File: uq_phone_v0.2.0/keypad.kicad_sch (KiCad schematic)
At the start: 71 parts, among them SW1 SKTAAAE010, SW10 SKTAAAE010, SW11 SKTAAAE010, SW12 SKTAAAE010, SW13 SKTAAAE010, SW14 SKTAAAE010, SW15 SKTAAAE010, SW16 SKSCLCE010, SW17 SKTAAAE010, SW18 SKTAAAE010, SW19 SKTAAAE010, SW2 SKTAAAE010, SW20 SKTAAAE010, SW21 SKTAAAE010, SW22 SKSCLCE010, SW23 SKTAAAE010, SW24 SKTAAAE010, SW25 SKTAAAE010, SW26 SKTAAAE010, SW27 SKTAAAE010, SW28 SKTAAAE010, SW29 SKTAAAE010, SW3 SKTAAAE010, SW30 SKTAAAE010, SW31 SKTAAAE010, SW32 SKTAAAE010, SW33 SKTAAAE010, SW34 SKTAAAE010, SW35 SKTAAAE010, SW36 SKTAAAE010, SW37 SKTAAAE010, SW38 SKTAAAE010, SW39 SKTAAAE010, SW4 SKTAAAE010, SW40 SKTAAAE010, SW41 SKTAAAE010, SW5 SKTAAAE010, SW6 SKSCLCE010, SW7 SKTAAAE010, SW8 SKTAAAE010, SW9 SKTAAAE010

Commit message: More routing and moving cellular to new project
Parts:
- LED18, LED19, LED20, LED21, LED22, LED23, LED24, LED25, LED26, LED27, LED28, LED31: now fitted
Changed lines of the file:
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@@
 		(in_bom yes)
 		(on_board yes)
-		(dnp yes)
+		(dnp no)
 		(property "Reference" "LED27"
 			(at 300.482 133.096 0)
@@
 		(in_bom yes)
 		(on_board yes)
-		(dnp yes)
+		(dnp no)
 		(fields_autoplaced yes)
 		(property "Reference" "#PWR0199"
@@
 		(in_bom yes)
 		(on_board yes)
-		(dnp yes)
+		(dnp no)
 		(property "Reference" "#PWR0212"
 			(at 313.69 129.54 0)
@@
 		(in_bom yes)
 		(on_board yes)
-		(dnp yes)
+		(dnp no)
 		(fields_autoplaced yes)
 		(property "Reference" "#PWR0201"
@@
 		(in_bom yes)
 		(on_board yes)
-		(dnp yes)
+		(dnp no)
 		(property "Reference" "#PWR0197"
 			(at 292.1 105.41 0)
@@
 		(in_bom yes)
 		(on_board yes)
-		(dnp yes)
+		(dnp no)
 		(fields_autoplaced yes)
 		(property "Reference" "#PWR0193"
@@
 		(in_bom yes)
 		(on_board yes)
-		(dnp yes)
+		(dnp no)
 		(property "Reference" "#PWR0218"
 			(at 313.69 153.67 0)
@@
 		(in_bom yes)
 		(on_board yes)
-		(dnp yes)
+		(dnp no)
 		(property "Reference" "#PWR0191"
 			(at 270.51 81.28 0)
@@
 		(in_bom yes)
 		(on_board yes)
-		(dnp yes)
+		(dnp no)
 		(property "Reference" "#PWR0208"
 			(at 292.1 129.54 0)
@@
 		(in_bom yes)
 		(on_board yes)
-		(dnp yes)
+		(dnp no)
 		(property "Reference" "LED25"
 			(at 322.072 108.966 0)
@@
 		(in_bom yes)
 		(on_board yes)
-		(dnp yes)
+		(dnp no)
 		(fields_autoplaced yes)
 		(property "Reference" "#PWR0200"
@@
 		(in_bom yes)
 		(on_board yes)
-		(dnp yes)
+		(dnp no)
 		(property "Reference" "#PWR0216"
 			(at 270.51 153.67 0)
@@
 		(in_bom yes)
 		(on_board yes)
-		(dnp yes)
+		(dnp no)
 		(property "Reference" "#PWR0217"
 			(at 292.1 153.67 0)
@@
 		(in_bom yes)
 		(on_board yes)
-		(dnp yes)
+		(dnp no)
 		(property "Reference" "LED23"
 			(at 278.892 108.966 0)
@@
 		(in_bom yes)
 		(on_board yes)
-		(dnp yes)
+		(dnp no)
 		(fields_autoplaced yes)
 		(property "Reference" "#PWR077"
@@
 		(in_bom yes)
 		(on_board yes)
-		(dnp yes)
+		(dnp no)
 		(property "Reference" "LED19"
 			(at 300.482 60.706 0)
@@
 		(in_bom yes)
 		(on_board yes)
-		(dnp yes)
+		(dnp no)
 		(property "Reference" "LED18"
 			(at 278.892 60.706 0)
@@
 		(in_bom yes)
 		(on_board yes)
-		(dnp yes)
+		(dnp no)
 		(fields_autoplaced yes)
 		(property "Reference" "#PWR0215"
@@
 		(in_bom yes)
 		(on_board yes)
-		(dnp yes)
+		(dnp no)
 		(property "Reference" "#PWR0198"
 			(at 313.69 105.41 0)
@@
 		(in_bom yes)
 		(on_board yes)
-		(dnp yes)
+		(dnp no)
 		(property "Reference" "LED24"
 			(at 300.482 108.966 0)
@@
 		(in_bom yes)
 		(on_board yes)
-		(dnp yes)
+		(dnp no)
 		(property "Reference" "LED26"
 			(at 278.892 133.096 0)
@@
 		(in_bom yes)
 		(on_board yes)
-		(dnp yes)
+		(dnp no)
 		(property "Reference" "#PWR0224"
 			(at 313.69 177.8 0)
@@
 		(in_bom yes)
 		(on_board yes)
-		(dnp yes)
+		(dnp no)
 		(fields_autoplaced yes)
 		(property "Reference" "#PWR0213"
@@
 		(in_bom yes)
 		(on_board yes)
-		(dnp yes)
+		(dnp no)
 		(property "Reference" "LED22"
 			(at 322.072 84.836 0)
@@
 		(in_bom yes)
 		(on_board yes)
-		(dnp yes)
+		(dnp no)
 		(fields_autoplaced yes)
 		(property "Reference" "#PWR0214"
@@
 		(in_bom yes)
 		(on_board yes)
-		(dnp yes)
+		(dnp no)
 		(property "Reference" "#PWR0202"
 			(at 270.51 129.54 0)
@@
 		(in_bom yes)
 		(on_board yes)
-		(dnp yes)
+		(dnp no)
 		(property "Reference" "LED28"
 			(at 322.072 133.096 0)
@@
 		(in_bom yes)
 		(on_board yes)
-		(dnp yes)
+		(dnp no)
 		(fields_autoplaced yes)
 		(property "Reference" "#PWR0192"
@@
 		(in_bom yes)
 		(on_board yes)
-		(dnp yes)
+		(dnp no)
 		(fields_autoplaced yes)
 		(property "Reference" "#PWR0221"
@@
 		(in_bom yes)
 		(on_board yes)
-		(dnp yes)
+		(dnp no)
 		(fields_autoplaced yes)
 		(property "Reference" "#PWR0194"
@@
 		(in_bom yes)
 		(on_board yes)
-		(dnp yes)
+		(dnp no)
 		(property "Reference" "LED31"
 			(at 322.072 157.226 0)
@@
 		(in_bom yes)
 		(on_board yes)
-		(dnp yes)
+		(dnp no)
 		(property "Reference" "#PWR0182"
 			(at 292.1 81.28 0)
@@
 		(in_bom yes)
 		(on_board yes)
-		(dnp yes)
+		(dnp no)
 		(property "Reference" "LED20"
 			(at 278.892 84.836 0)
@@
 		(in_bom yes)
 		(on_board yes)
-		(dnp yes)
+		(dnp no)
 		(property "Reference" "LED21"
 			(at 300.482 84.836 0)
@@
 		(in_bom yes)
 		(on_board yes)
-		(dnp yes)
+		(dnp no)
 		(fields_autoplaced yes)
 		(property "Reference" "#PWR0195"
@@
 		(in_bom yes)
 		(on_board yes)
-		(dnp yes)
+		(dnp no)
 		(property "Reference" "#PWR0196"
 			(at 270.51 105.41 0)

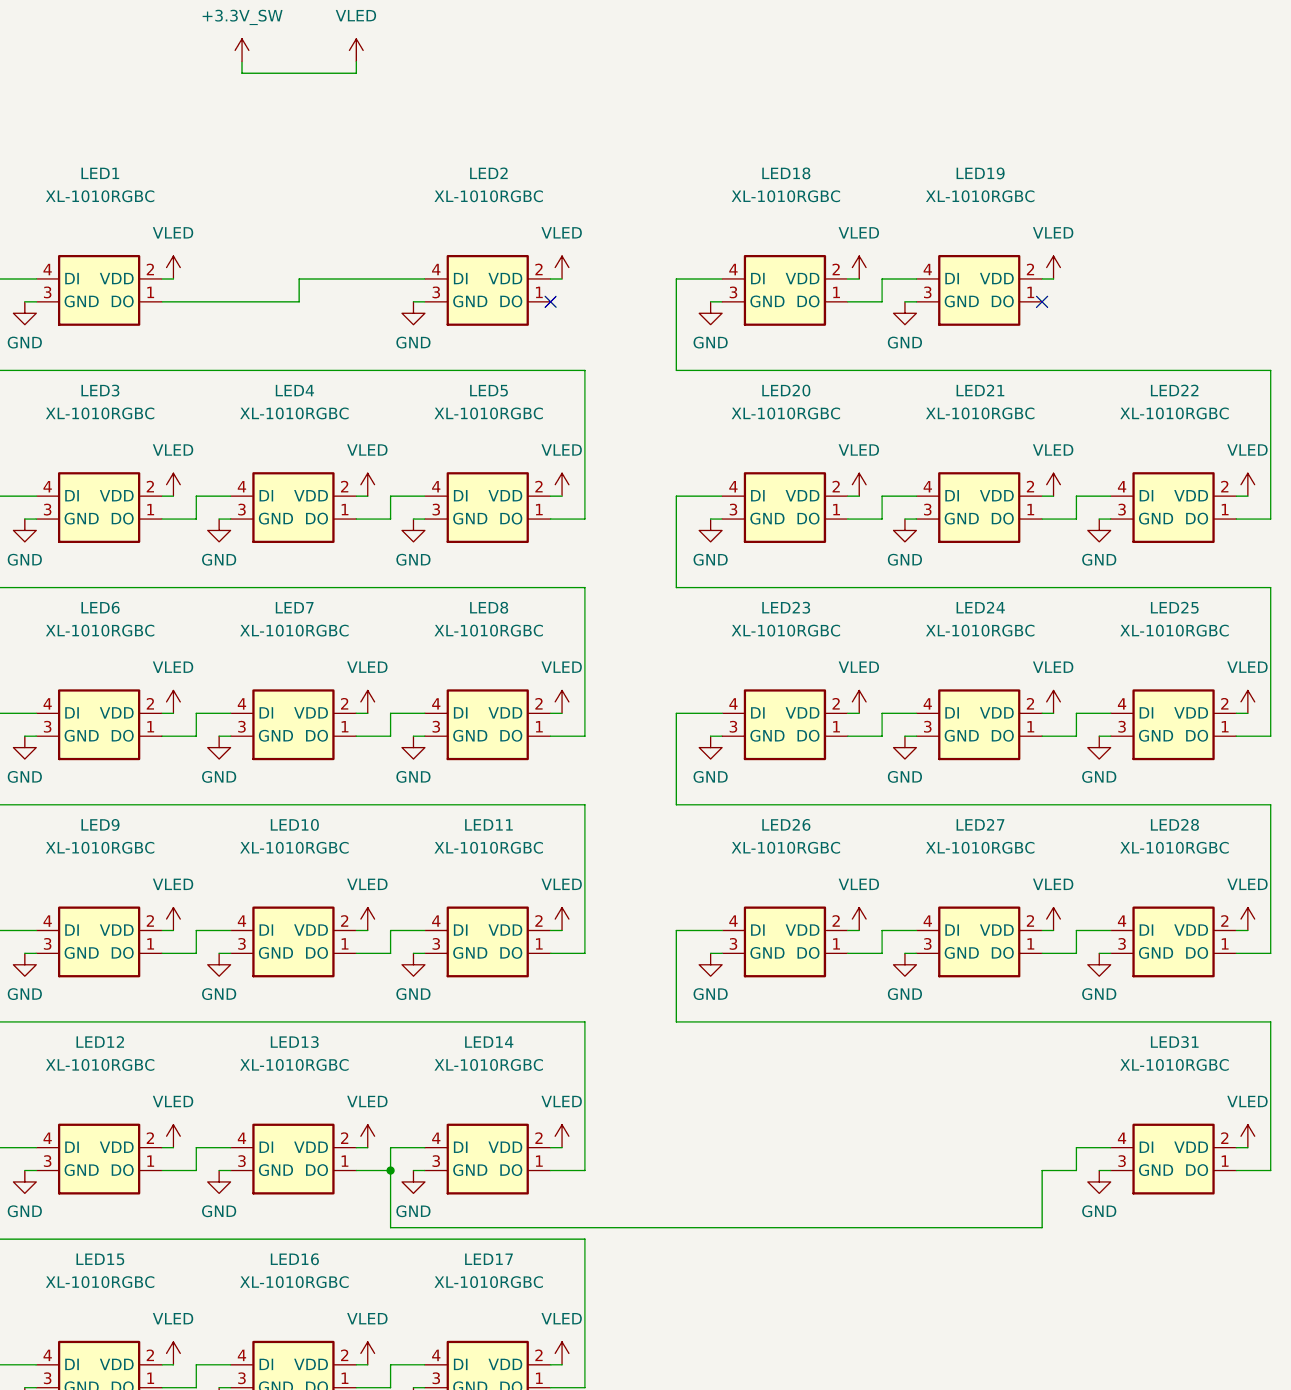
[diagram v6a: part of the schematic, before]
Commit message: New HP jack and circuit
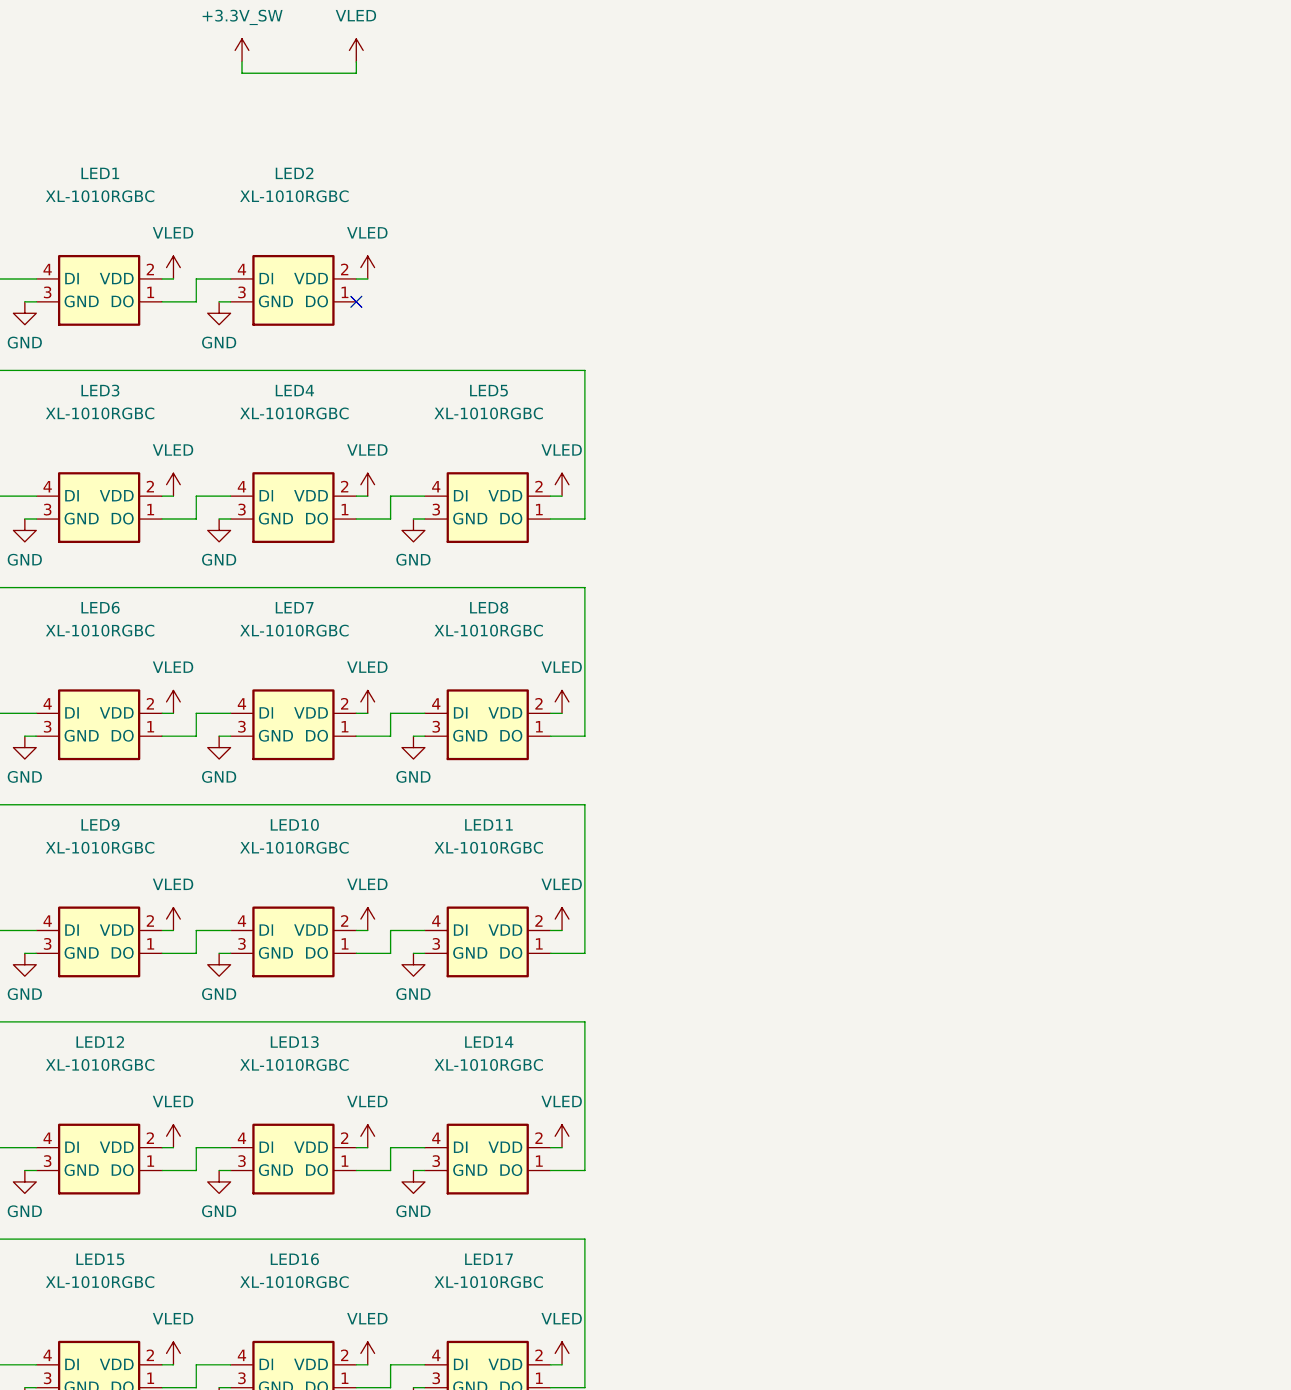
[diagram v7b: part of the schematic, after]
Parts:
- removed LED1, LED10, LED11, LED14, LED2, LED3, LED4, LED5, LED6, LED7, LED8, LED9: XL-1010RGBC, custom_footprints:XL-1010RGBC-WS2812B, symbol Misc:XL-1010RGBC-WS2812B
- renumbered LED18 to LED1, LED27 to LED10, LED28 to LED11, LED31 to LED14, LED19 to LED2, LED20 to LED3, LED21 to LED4, LED22 to LED5, LED23 to LED6, LED24 to LED7, LED25 to LED8, LED26 to LED9
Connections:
- no-connect marks 2 -> 1
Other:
- moved on the sheet: LED1, LED10, LED11, LED14, LED2, LED3, LED4, LED5, LED6, LED7, LED8, LED9
